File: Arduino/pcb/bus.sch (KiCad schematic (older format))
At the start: 0 parts

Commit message: pcb: continue wiring / move parts to hierachival sheets
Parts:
- added C1, C2: 100nF, symbol Device:C
- added J4, J6: Floppy-Bus, symbol floppy-bus-connector:Floppy-Bus
- added J5: MAX485 Socket, Housings_DIP:DIP-8_W7.62mm, symbol Interface_UART:MAX485E
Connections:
- new net: J4.7 (BM), J5.6 (A)
- new net: J4.9 (Pin_9), J5.7 (B)
- new net: J4.10 (Pin_10), J6.9 (Pin_9)
- new net: J4.2 (20V), J6.1 (20V)
- new net: J4.4 (GND), J6.3 (GND)
- new net: J4.8 (BM), J6.7 (BM)
- new net BUS_POWER: J4.1 (20V)
- new net GND: C1.2, C2.2, J4.3 (GND), J5.2 (~RE), J5.3 (DE), J5.5 (GND)
- new net RX: J5.4 (DI)
- new net TX: J5.1 (RO)
- new net VCC: C1.1, C2.1, J5.8 (VCC)
- no-connect marks 0 -> 4
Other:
- note added: "Bypass"
- note added: "Output to next module"
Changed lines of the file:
@@
 $Descr A4 11693 8268
 encoding utf-8
-Sheet 1 6
+Sheet 3 6
 Title ""
 Date ""
@@
 Comment4 ""
 $EndDescr
+$Comp
+L Interface_UART:MAX485E J5
+U 1 1 5CF1EB96
+P 7275 3925
+F 0 "J5" H 6900 4525 50  0000 C CNN
+F 1 "MAX485 Socket" H 6875 4425 50  0000 C CNN
+F 2 "Housings_DIP:DIP-8_W7.62mm" H 7275 3925 50  0001 C CNN
+F 3 "" H 7275 3925 50  0001 C CNN
+	1    7275 3925
+	-1   0    0    -1
+$EndComp
+Wire Wire Line
+	7625 2475 8325 2475
+Wire Wire Line
+	7625 2675 8325 2675
+Wire Wire Line
+	7625 2775 8325 2775
+NoConn ~ 9125 2375
+NoConn ~ 9125 2475
+NoConn ~ 9125 2675
+NoConn ~ 9125 2775
+Text Notes 8325 2950 0    50   ~ 0
+Output to next module
+$Comp
+L power:GND #PWR011
+U 1 1 5CF1EBB2
+P 6575 2925
+F 0 "#PWR011" H 6575 2675 50  0001 C CNN
+F 1 "GND" H 6580 2752 50  0000 C CNN
+F 2 "" H 6575 2925 50  0001 C CNN
+F 3 "" H 6575 2925 50  0001 C CNN
+	1    6575 2925
+	1    0    0    -1
+$EndComp
+Wire Wire Line
+	6825 2475 6575 2475
+Wire Wire Line
+	6575 2475 6575 2925
+$Comp
+L power:VCC #PWR012
+U 1 1 5CF1EBBB
+P 7275 3325
+F 0 "#PWR012" H 7275 3175 50  0001 C CNN
+F 1 "VCC" H 7292 3498 50  0000 C CNN
+F 2 "" H 7275 3325 50  0001 C CNN
+F 3 "" H 7275 3325 50  0001 C CNN
+	1    7275 3325
+	1    0    0    -1
+$EndComp
+$Comp
+L power:GND #PWR013
+U 1 1 5CF1EBC1
+P 7275 4625
+F 0 "#PWR013" H 7275 4375 50  0001 C CNN
+F 1 "GND" H 7280 4452 50  0000 C CNN
+F 2 "" H 7275 4625 50  0001 C CNN
+F 3 "" H 7275 4625 50  0001 C CNN
+	1    7275 4625
+	1    0    0    -1
+$EndComp
+Wire Wire Line
+	6825 2675 6775 2675
+Wire Wire Line
+	7275 3425 7275 3325
+Wire Wire Line
+	7275 4525 7275 4625
+Wire Wire Line
+	6825 2775 6825 3825
+Wire Wire Line
+	6825 3825 6875 3825
+Wire Wire Line
+	6775 2675 6775 4125
+Wire Wire Line
+	6775 4125 6875 4125
+Wire Wire Line
+	7675 3825 7925 3825
+Wire Wire Line
+	7675 4125 7925 4125
+Wire Wire Line
+	7675 4025 8425 4025
+Wire Wire Line
+	7675 3925 8425 3925
+Wire Wire Line
+	8425 3925 8425 4025
+Connection ~ 8425 4025
+$Comp
+L power:GND #PWR014
+U 1 1 5CF1EBD6
+P 8425 4125
+F 0 "#PWR014" H 8425 3875 50  0001 C CNN
+F 1 "GND" H 8430 3952 50  0000 C CNN
+F 2 "" H 8425 4125 50  0001 C CNN
+F 3 "" H 8425 4125 50  0001 C CNN
+	1    8425 4125
+	1    0    0    -1
+$EndComp
+Wire Wire Line
+	8425 4025 8425 4125
+Text HLabel 7925 3825 2    50   Output ~ 0
+TX
+Text HLabel 7925 4125 2    50   Input ~ 0
+RX
+Text HLabel 6575 2375 0    50   Output ~ 0
+BUS_POWER
+$Comp
+L Device:C C?
+U 1 1 5D17F33C
+P 6300 4750
+AR Path="/5D17F33C" Ref="C?"  Part="1"
+AR Path="/5CCFEC3E/5D17F33C" Ref="C?"  Part="1"
+AR Path="/5CD1E0A5/5D17F33C" Ref="C1"  Part="1"
+F 0 "C1" H 6075 4950 50  0000 L CNN
+F 1 "100nF" H 6025 4850 50  0000 L CNN
+F 2 "" H 6338 4600 50  0001 C CNN
+F 3 "~" H 6300 4750 50  0001 C CNN
+	1    6300 4750
+	1    0    0    -1
+$EndComp
+$Comp
+L power:VCC #PWR?
+U 1 1 5D17F342
+P 6300 4475
+AR Path="/5CCFEC3E/5D17F342" Ref="#PWR?"  Part="1"
+AR Path="/5CD1E0A5/5D17F342" Ref="#PWR09"  Part="1"
+F 0 "#PWR09" H 6300 4325 50  0001 C CNN
+F 1 "VCC" H 6317 4648 50  0000 C CNN
+F 2 "" H 6300 4475 50  0001 C CNN
+F 3 "" H 6300 4475 50  0001 C CNN
+	1    6300 4475
+	1    0    0    -1
+$EndComp
+$Comp
+L power:GND #PWR?
+U 1 1 5D17F348
+P 6300 5000
+AR Path="/5CCFEC3E/5D17F348" Ref="#PWR?"  Part="1"
+AR Path="/5CD1E0A5/5D17F348" Ref="#PWR010"  Part="1"
+F 0 "#PWR010" H 6300 4750 50  0001 C CNN
+F 1 "GND" H 6305 4827 50  0000 C CNN
+F 2 "" H 6300 5000 50  0001 C CNN
+F 3 "" H 6300 5000 50  0001 C CNN
+	1    6300 5000
+	1    0    0    -1
+$EndComp
+Wire Wire Line
+	6300 4475 6300 4600
+Wire Wire Line
+	6300 4900 6300 5000
+Text Notes 5925 4425 0    50   ~ 0
+Bypass
+$Comp
+L Device:C C?
+U 1 1 5D182EF8
+P 6600 4750
+AR Path="/5D182EF8" Ref="C?"  Part="1"
+AR Path="/5CCFEC3E/5D182EF8" Ref="C?"  Part="1"
+AR Path="/5CD1E0A5/5D182EF8" Ref="C2"  Part="1"
+F 0 "C2" H 6375 4950 50  0000 L CNN
+F 1 "100nF" H 6325 4850 50  0000 L CNN
+F 2 "" H 6638 4600 50  0001 C CNN
+F 3 "~" H 6600 4750 50  0001 C CNN
+	1    6600 4750
+	1    0    0    -1
+$EndComp
+Wire Wire Line
+	6600 4475 6600 4600
+Wire Wire Line
+	6600 4900 6600 5000
+Wire Wire Line
+	6600 4475 6300 4475
+Connection ~ 6300 4475
+Wire Wire Line
+	6600 5000 6300 5000
+Connection ~ 6300 5000
+$Comp
+L floppy-bus-connector:Floppy-Bus J4
+U 1 1 5D1AADEF
+P 7025 2575
+F 0 "J4" H 7225 2992 50  0000 C CNN
+F 1 "Floppy-Bus" H 7225 2901 50  0000 C CNN
+F 2 "" H 7025 2575 50  0001 C CNN
+F 3 "" H 7025 2575 50  0001 C CNN
+	1    7025 2575
+	1    0    0    -1
+$EndComp
+$Comp
+L floppy-bus-connector:Floppy-Bus J6
+U 1 1 5D1ABE61
+P 8525 2575
+F 0 "J6" H 8725 2992 50  0000 C CNN
+F 1 "Floppy-Bus" H 8725 2901 50  0000 C CNN
+F 2 "" H 8525 2575 50  0001 C CNN
+F 3 "" H 8525 2575 50  0001 C CNN
+	1    8525 2575
+	1    0    0    -1
+$EndComp
+Wire Wire Line
+	6575 2375 6725 2375
+$Comp
+L power:PWR_FLAG #FLG01
+U 1 1 5D1B34B5
+P 6725 2375
+F 0 "#FLG01" H 6725 2450 50  0001 C CNN
+F 1 "PWR_FLAG" H 6725 2548 50  0000 C CNN
+F 2 "" H 6725 2375 50  0001 C CNN
+F 3 "~" H 6725 2375 50  0001 C CNN
+	1    6725 2375
+	1    0    0    -1
+$EndComp
+Connection ~ 6725 2375
+Wire Wire Line
+	6725 2375 6825 2375
+Wire Wire Line
+	7625 2375 8325 2375
 $EndSCHEMATC

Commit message: pcb: finish wiring / use ws2812 under chip led
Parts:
- renumbered J4 to J2, J5 to J3, J6 to J4
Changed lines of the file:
@@
 $Descr A4 11693 8268
 encoding utf-8
-Sheet 3 6
+Sheet 2 6
 Title ""
 Date ""
@@
 $EndDescr
 $Comp
-L Interface_UART:MAX485E J5
+L Interface_UART:MAX485E J3
 U 1 1 5CF1EB96
 P 7275 3925
-F 0 "J5" H 6900 4525 50  0000 C CNN
+F 0 "J3" H 6900 4525 50  0000 C CNN
 F 1 "MAX485 Socket" H 6875 4425 50  0000 C CNN
 F 2 "Housings_DIP:DIP-8_W7.62mm" H 7275 3925 50  0001 C CNN
@@
 Output to next module
 $Comp
-L power:GND #PWR011
+L power:GND #PWR04
 U 1 1 5CF1EBB2
 P 6575 2925
-F 0 "#PWR011" H 6575 2675 50  0001 C CNN
+F 0 "#PWR04" H 6575 2675 50  0001 C CNN
 F 1 "GND" H 6580 2752 50  0000 C CNN
 F 2 "" H 6575 2925 50  0001 C CNN
@@
 	6575 2475 6575 2925
 $Comp
-L power:VCC #PWR012
+L power:VCC #PWR05
 U 1 1 5CF1EBBB
 P 7275 3325
-F 0 "#PWR012" H 7275 3175 50  0001 C CNN
+F 0 "#PWR05" H 7275 3175 50  0001 C CNN
 F 1 "VCC" H 7292 3498 50  0000 C CNN
 F 2 "" H 7275 3325 50  0001 C CNN
@@
 $EndComp
 $Comp
-L power:GND #PWR013
+L power:GND #PWR06
 U 1 1 5CF1EBC1
 P 7275 4625
-F 0 "#PWR013" H 7275 4375 50  0001 C CNN
+F 0 "#PWR06" H 7275 4375 50  0001 C CNN
 F 1 "GND" H 7280 4452 50  0000 C CNN
 F 2 "" H 7275 4625 50  0001 C CNN
@@
 Connection ~ 8425 4025
 $Comp
-L power:GND #PWR014
+L power:GND #PWR07
 U 1 1 5CF1EBD6
 P 8425 4125
-F 0 "#PWR014" H 8425 3875 50  0001 C CNN
+F 0 "#PWR07" H 8425 3875 50  0001 C CNN
 F 1 "GND" H 8430 3952 50  0000 C CNN
 F 2 "" H 8425 4125 50  0001 C CNN
@@
 P 6300 4475
 AR Path="/5CCFEC3E/5D17F342" Ref="#PWR?"  Part="1"
-AR Path="/5CD1E0A5/5D17F342" Ref="#PWR09"  Part="1"
-F 0 "#PWR09" H 6300 4325 50  0001 C CNN
+AR Path="/5CD1E0A5/5D17F342" Ref="#PWR02"  Part="1"
+F 0 "#PWR02" H 6300 4325 50  0001 C CNN
 F 1 "VCC" H 6317 4648 50  0000 C CNN
 F 2 "" H 6300 4475 50  0001 C CNN
@@
 P 6300 5000
 AR Path="/5CCFEC3E/5D17F348" Ref="#PWR?"  Part="1"
-AR Path="/5CD1E0A5/5D17F348" Ref="#PWR010"  Part="1"
-F 0 "#PWR010" H 6300 4750 50  0001 C CNN
+AR Path="/5CD1E0A5/5D17F348" Ref="#PWR03"  Part="1"
+F 0 "#PWR03" H 6300 4750 50  0001 C CNN
 F 1 "GND" H 6305 4827 50  0000 C CNN
 F 2 "" H 6300 5000 50  0001 C CNN
@@
 Connection ~ 6300 5000
 $Comp
-L floppy-bus-connector:Floppy-Bus J4
+L floppy-bus-connector:Floppy-Bus J2
 U 1 1 5D1AADEF
 P 7025 2575
-F 0 "J4" H 7225 2992 50  0000 C CNN
+F 0 "J2" H 7225 2992 50  0000 C CNN
 F 1 "Floppy-Bus" H 7225 2901 50  0000 C CNN
 F 2 "" H 7025 2575 50  0001 C CNN
@@
 $EndComp
 $Comp
-L floppy-bus-connector:Floppy-Bus J6
+L floppy-bus-connector:Floppy-Bus J4
 U 1 1 5D1ABE61
 P 8525 2575
-F 0 "J6" H 8725 2992 50  0000 C CNN
+F 0 "J4" H 8725 2992 50  0000 C CNN
 F 1 "Floppy-Bus" H 8725 2901 50  0000 C CNN
 F 2 "" H 8525 2575 50  0001 C CNN

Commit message: pcb: assign footprints
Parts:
- C1, C2: footprint (none) -> Capacitor_SMD:C_0201_0603Metric
- J2, J4: footprint (none) -> shrouded:Shrouded_Header_2x05_Pitch2.54mm
- J3: footprint Housings_DIP:DIP-8_W7.62mm -> Package_DIP:DIP-8_W7.62mm
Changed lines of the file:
@@
 F 0 "J3" H 6900 4525 50  0000 C CNN
 F 1 "MAX485 Socket" H 6875 4425 50  0000 C CNN
-F 2 "Housings_DIP:DIP-8_W7.62mm" H 7275 3925 50  0001 C CNN
+F 2 "Package_DIP:DIP-8_W7.62mm" H 7275 3925 50  0001 C CNN
 F 3 "" H 7275 3925 50  0001 C CNN
 	1    7275 3925
@@
 F 0 "C1" H 6075 4950 50  0000 L CNN
 F 1 "100nF" H 6025 4850 50  0000 L CNN
-F 2 "" H 6338 4600 50  0001 C CNN
+F 2 "Capacitor_SMD:C_0201_0603Metric" H 6338 4600 50  0001 C CNN
 F 3 "~" H 6300 4750 50  0001 C CNN
 	1    6300 4750
@@
 F 0 "C2" H 6375 4950 50  0000 L CNN
 F 1 "100nF" H 6325 4850 50  0000 L CNN
-F 2 "" H 6638 4600 50  0001 C CNN
+F 2 "Capacitor_SMD:C_0201_0603Metric" H 6638 4600 50  0001 C CNN
 F 3 "~" H 6600 4750 50  0001 C CNN
 	1    6600 4750
@@
 F 0 "J2" H 7225 2992 50  0000 C CNN
 F 1 "Floppy-Bus" H 7225 2901 50  0000 C CNN
-F 2 "" H 7025 2575 50  0001 C CNN
+F 2 "shrouded:Shrouded_Header_2x05_Pitch2.54mm" H 7025 2575 50  0001 C CNN
 F 3 "" H 7025 2575 50  0001 C CNN
 	1    7025 2575
@@
 F 0 "J4" H 8725 2992 50  0000 C CNN
 F 1 "Floppy-Bus" H 8725 2901 50  0000 C CNN
-F 2 "" H 8525 2575 50  0001 C CNN
+F 2 "shrouded:Shrouded_Header_2x05_Pitch2.54mm" H 8525 2575 50  0001 C CNN
 F 3 "" H 8525 2575 50  0001 C CNN
 	1    8525 2575

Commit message: pcb: add SOIC-8 socket footprint + 3D model
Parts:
- J3: footprint Package_DIP:DIP-8_W7.62mm -> dil:dil_8-300_socket
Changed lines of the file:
@@
 F 0 "J3" H 6900 4525 50  0000 C CNN
 F 1 "MAX485 Socket" H 6875 4425 50  0000 C CNN
-F 2 "Package_DIP:DIP-8_W7.62mm" H 7275 3925 50  0001 C CNN
+F 2 "dil:dil_8-300_socket" H 7275 3925 50  0001 C CNN
 F 3 "" H 7275 3925 50  0001 C CNN
 	1    7275 3925

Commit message: pcb: continue placement + add some info on silk
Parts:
- removed C2: 100nF, Capacitor_SMD:C_0201_0603Metric, symbol Device:C
- C1: footprint Capacitor_SMD:C_0201_0603Metric -> Capacitor_SMD:C_0805_2012Metric
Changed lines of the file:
@@
 F 0 "C1" H 6075 4950 50  0000 L CNN
 F 1 "100nF" H 6025 4850 50  0000 L CNN
-F 2 "Capacitor_SMD:C_0201_0603Metric" H 6338 4600 50  0001 C CNN
+F 2 "Capacitor_SMD:C_0805_2012Metric" H 6338 4600 50  0001 C CNN
 F 3 "~" H 6300 4750 50  0001 C CNN
 	1    6300 4750
@@
 Bypass
 $Comp
-L Device:C C?
-U 1 1 5D182EF8
-P 6600 4750
-AR Path="/5D182EF8" Ref="C?"  Part="1"
-AR Path="/5CCFEC3E/5D182EF8" Ref="C?"  Part="1"
-AR Path="/5CD1E0A5/5D182EF8" Ref="C2"  Part="1"
-F 0 "C2" H 6375 4950 50  0000 L CNN
-F 1 "100nF" H 6325 4850 50  0000 L CNN
-F 2 "Capacitor_SMD:C_0201_0603Metric" H 6638 4600 50  0001 C CNN
-F 3 "~" H 6600 4750 50  0001 C CNN
-	1    6600 4750
-	1    0    0    -1
-$EndComp
-Wire Wire Line
-	6600 4475 6600 4600
-Wire Wire Line
-	6600 4900 6600 5000
-Wire Wire Line
-	6600 4475 6300 4475
-Connection ~ 6300 4475
-Wire Wire Line
-	6600 5000 6300 5000
-Connection ~ 6300 5000
-$Comp
 L floppy-bus-connector:Floppy-Bus J2

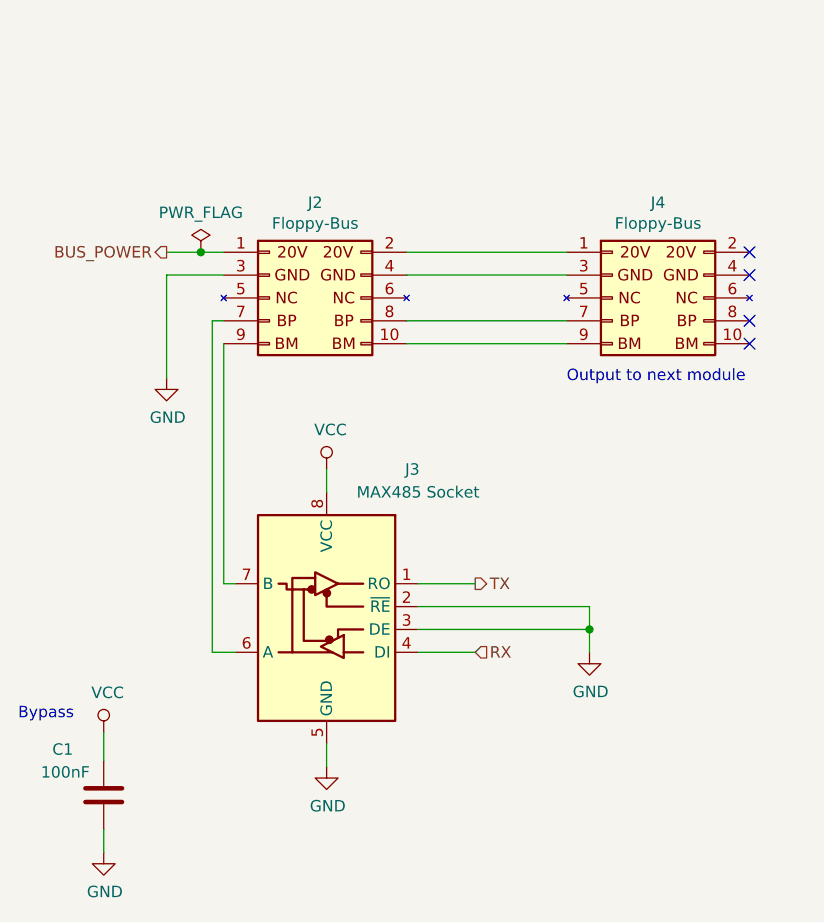
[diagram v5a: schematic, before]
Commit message: pcb: fix bus wiring, add bus silk pin descriptions
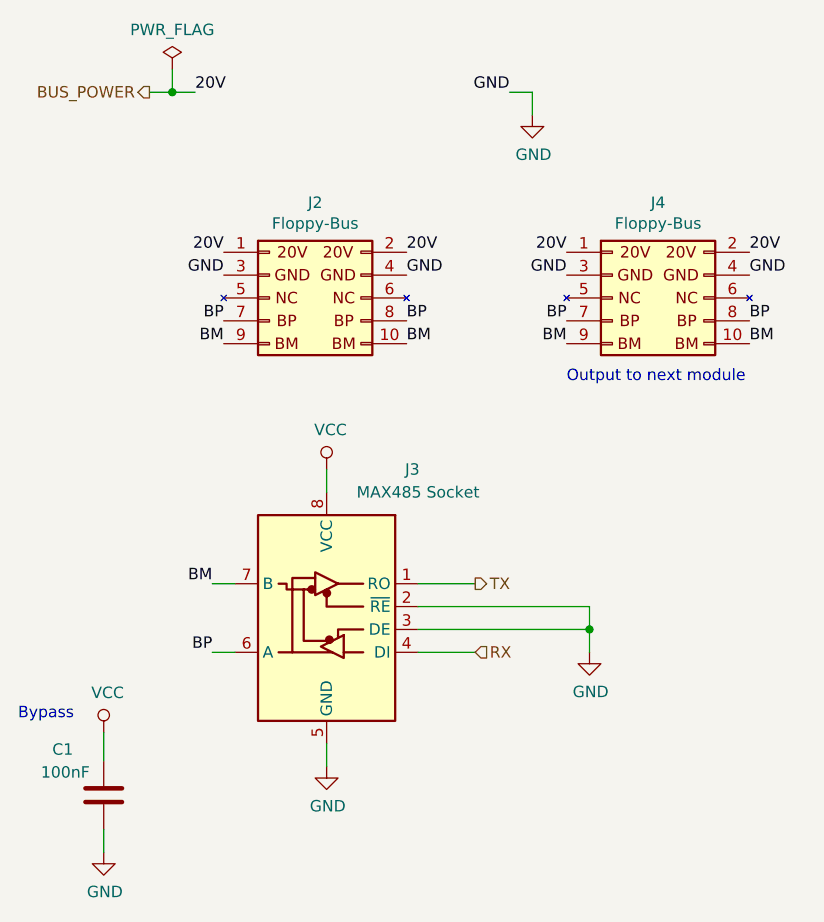
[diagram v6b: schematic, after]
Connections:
- net BUS_POWER: now also J2.2 (20V), J4.1 (20V), J4.2 (20V)
- net GND: now also J2.4 (GND), J4.3 (GND), J4.4 (GND)
- net BP: now reaches J2.7 (BM), J3.6 (A)
- net BP: now also J2.8 (BM), J4.7 (BM), J4.8 (BM)
- net BM: now reaches J2.9 (Pin_9), J3.7 (B)
- net BM: now also J2.10 (Pin_10), J4.10 (Pin_10), J4.9 (Pin_9)
- no-connect marks 4 -> 0
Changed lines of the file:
@@
 	-1   0    0    -1
 $EndComp
-Wire Wire Line
-	7625 2475 8325 2475
-Wire Wire Line
-	7625 2675 8325 2675
-Wire Wire Line
-	7625 2775 8325 2775
-NoConn ~ 9125 2375
-NoConn ~ 9125 2475
-NoConn ~ 9125 2675
-NoConn ~ 9125 2775
 Text Notes 8325 2950 0    50   ~ 0
 Output to next module
-$Comp
-L power:GND #PWR04
-U 1 1 5CF1EBB2
-P 6575 2925
-F 0 "#PWR04" H 6575 2675 50  0001 C CNN
-F 1 "GND" H 6580 2752 50  0000 C CNN
-F 2 "" H 6575 2925 50  0001 C CNN
-F 3 "" H 6575 2925 50  0001 C CNN
-	1    6575 2925
-	1    0    0    -1
-$EndComp
-Wire Wire Line
-	6825 2475 6575 2475
-Wire Wire Line
-	6575 2475 6575 2925
 $Comp
 L power:VCC #PWR05
@@
 $EndComp
 Wire Wire Line
-	6825 2675 6775 2675
-Wire Wire Line
 	7275 3425 7275 3325
 Wire Wire Line
 	7275 4525 7275 4625
-Wire Wire Line
-	6825 2775 6825 3825
-Wire Wire Line
-	6825 3825 6875 3825
-Wire Wire Line
-	6775 2675 6775 4125
-Wire Wire Line
-	6775 4125 6875 4125
 Wire Wire Line
 	7675 3825 7925 3825
@@
 Text HLabel 7925 4125 2    50   Input ~ 0
 RX
-Text HLabel 6575 2375 0    50   Output ~ 0
+Text HLabel 6500 1675 0    50   Output ~ 0
 BUS_POWER
 $Comp
@@
 Bypass
 $Comp
+L power:PWR_FLAG #FLG01
+U 1 1 5D1B34B5
+P 6600 1575
+F 0 "#FLG01" H 6600 1650 50  0001 C CNN
+F 1 "PWR_FLAG" H 6600 1748 50  0000 C CNN
+F 2 "" H 6600 1575 50  0001 C CNN
+F 3 "~" H 6600 1575 50  0001 C CNN
+	1    6600 1575
+	1    0    0    -1
+$EndComp
+Text Label 6700 1675 0    50   ~ 0
+20V
+Text Label 6775 4125 2    50   ~ 0
+BP
+Text Label 6775 3825 2    50   ~ 0
+BM
+Wire Wire Line
+	6700 1675 6600 1675
+Wire Wire Line
+	6500 1675 6600 1675
+Connection ~ 6600 1675
+$Comp
+L floppy-bus-connector:Floppy-Bus J4
+U 1 1 5D1ABE61
+P 8525 2575
+F 0 "J4" H 8725 2992 50  0000 C CNN
+F 1 "Floppy-Bus" H 8725 2901 50  0000 C CNN
+F 2 "shrouded:Shrouded_Header_2x05_Pitch2.54mm" H 8525 2575 50  0001 C CNN
+F 3 "" H 8525 2575 50  0001 C CNN
+	1    8525 2575
+	1    0    0    -1
+$EndComp
+Wire Wire Line
+	6600 1575 6600 1675
+Wire Wire Line
+	6875 3825 6775 3825
+Wire Wire Line
+	6875 4125 6775 4125
+Text Label 6825 2375 2    50   ~ 0
+20V
+Text Label 7625 2375 0    50   ~ 0
+20V
+Text Label 8325 2375 2    50   ~ 0
+20V
+Text Label 9125 2375 0    50   ~ 0
+20V
+$Comp
+L power:GND #PWR?
+U 1 1 5CDB5675
+P 8175 1775
+F 0 "#PWR?" H 8175 1525 50  0001 C CNN
+F 1 "GND" H 8180 1602 50  0000 C CNN
+F 2 "" H 8175 1775 50  0001 C CNN
+F 3 "" H 8175 1775 50  0001 C CNN
+	1    8175 1775
+	1    0    0    -1
+$EndComp
+Text Label 8075 1675 2    50   ~ 0
+GND
+Wire Wire Line
+	8075 1675 8175 1675
+Wire Wire Line
+	8175 1675 8175 1775
+Text Label 7625 2475 0    50   ~ 0
+GND
+Text Label 8325 2475 2    50   ~ 0
+GND
+Text Label 9125 2475 0    50   ~ 0
+GND
+Text Label 6825 2475 2    50   ~ 0
+GND
+$Comp
 L floppy-bus-connector:Floppy-Bus J2
 U 1 1 5D1AADEF
@@
 	1    0    0    -1
 $EndComp
-$Comp
-L floppy-bus-connector:Floppy-Bus J4
-U 1 1 5D1ABE61
-P 8525 2575
-F 0 "J4" H 8725 2992 50  0000 C CNN
-F 1 "Floppy-Bus" H 8725 2901 50  0000 C CNN
-F 2 "shrouded:Shrouded_Header_2x05_Pitch2.54mm" H 8525 2575 50  0001 C CNN
-F 3 "" H 8525 2575 50  0001 C CNN
-	1    8525 2575
-	1    0    0    -1
-$EndComp
-Wire Wire Line
-	6575 2375 6725 2375
-$Comp
-L power:PWR_FLAG #FLG01
-U 1 1 5D1B34B5
-P 6725 2375
-F 0 "#FLG01" H 6725 2450 50  0001 C CNN
-F 1 "PWR_FLAG" H 6725 2548 50  0000 C CNN
-F 2 "" H 6725 2375 50  0001 C CNN
-F 3 "~" H 6725 2375 50  0001 C CNN
-	1    6725 2375
-	1    0    0    -1
-$EndComp
-Connection ~ 6725 2375
-Wire Wire Line
-	6725 2375 6825 2375
-Wire Wire Line
-	7625 2375 8325 2375
+Text Label 6825 2675 2    50   ~ 0
+BP
+Text Label 6825 2775 2    50   ~ 0
+BM
+Text Label 7625 2675 0    50   ~ 0
+BP
+Text Label 9125 2675 0    50   ~ 0
+BP
+Text Label 8325 2675 2    50   ~ 0
+BP
+Text Label 8325 2775 2    50   ~ 0
+BM
+Text Label 7625 2775 0    50   ~ 0
+BM
+Text Label 9125 2775 0    50   ~ 0
+BM
 $EndSCHEMATC
